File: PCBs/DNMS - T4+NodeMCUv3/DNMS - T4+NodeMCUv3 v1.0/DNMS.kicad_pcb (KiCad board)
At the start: 2 copper layers, 61 x 32.5 mm, 20 parts, among them J1 Conn_02x03_Odd_Even, J2 Conn_01x02, J3 Conn_01x04, J4 Conn_01x05, U2 NodeMCU V3, U3 Teensy4.0

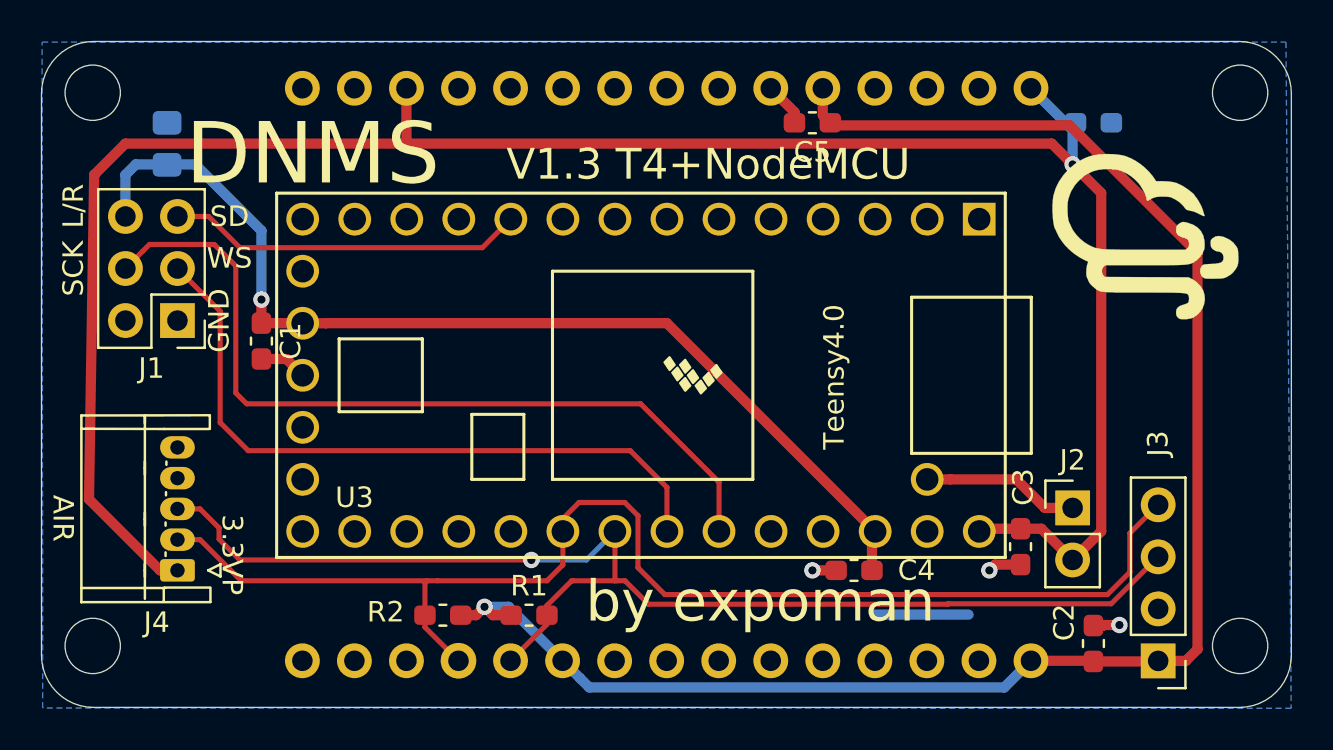
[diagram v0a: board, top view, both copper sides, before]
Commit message: move connectors
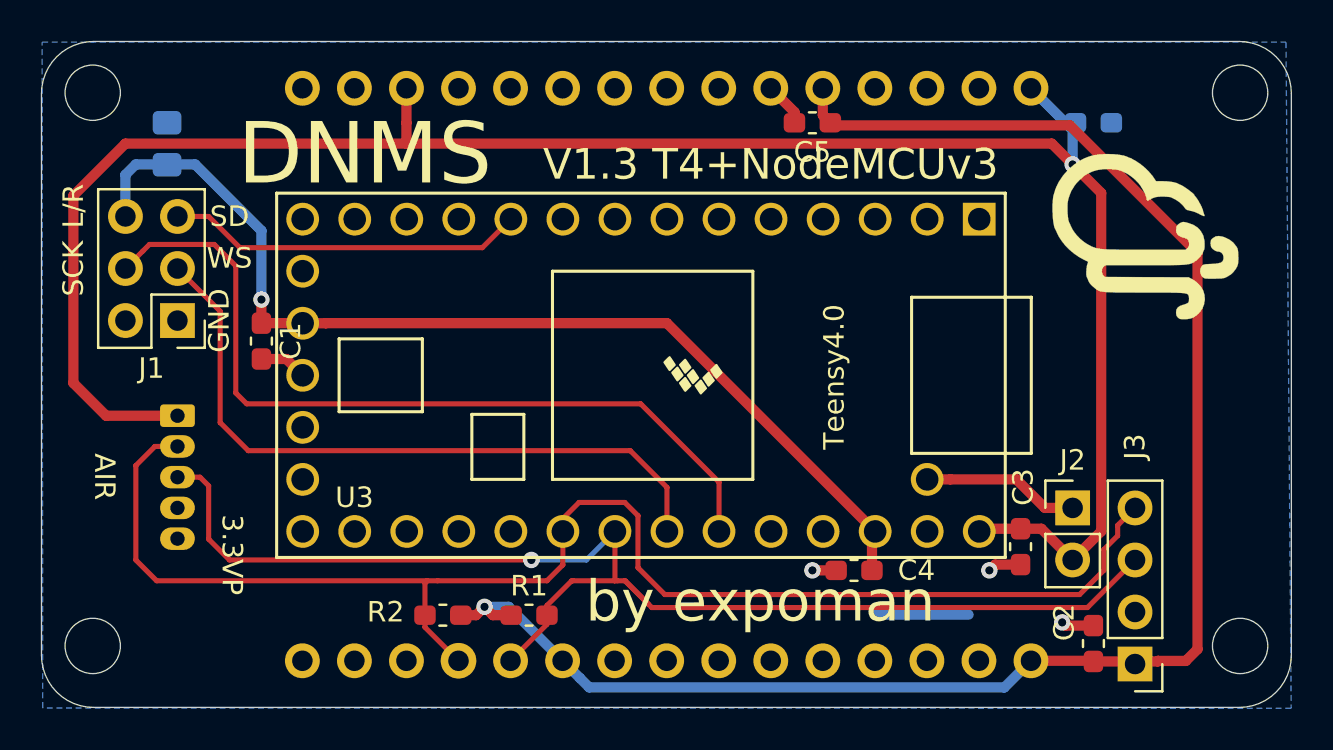
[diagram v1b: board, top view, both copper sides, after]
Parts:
- J4: moved to B.Cu
- moved J4 7.55 mm to (72.1, 75.8), turned to 270 degrees
- moved J3 1.14 mm to (118.9, 87.9)
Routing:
- net SDA: track 62.5 -> 69.7 mm
- net +5V: track 103.8 -> 98.5 mm
- net SCL: track 61.3 -> 63.7 mm
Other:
- board text added: "V1.3 T4+NodeMCUv3"
- board text removed: "V1.3 T4+NodeMCU"

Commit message: change connector to mic to molex pico-ezmate
move other connectors around
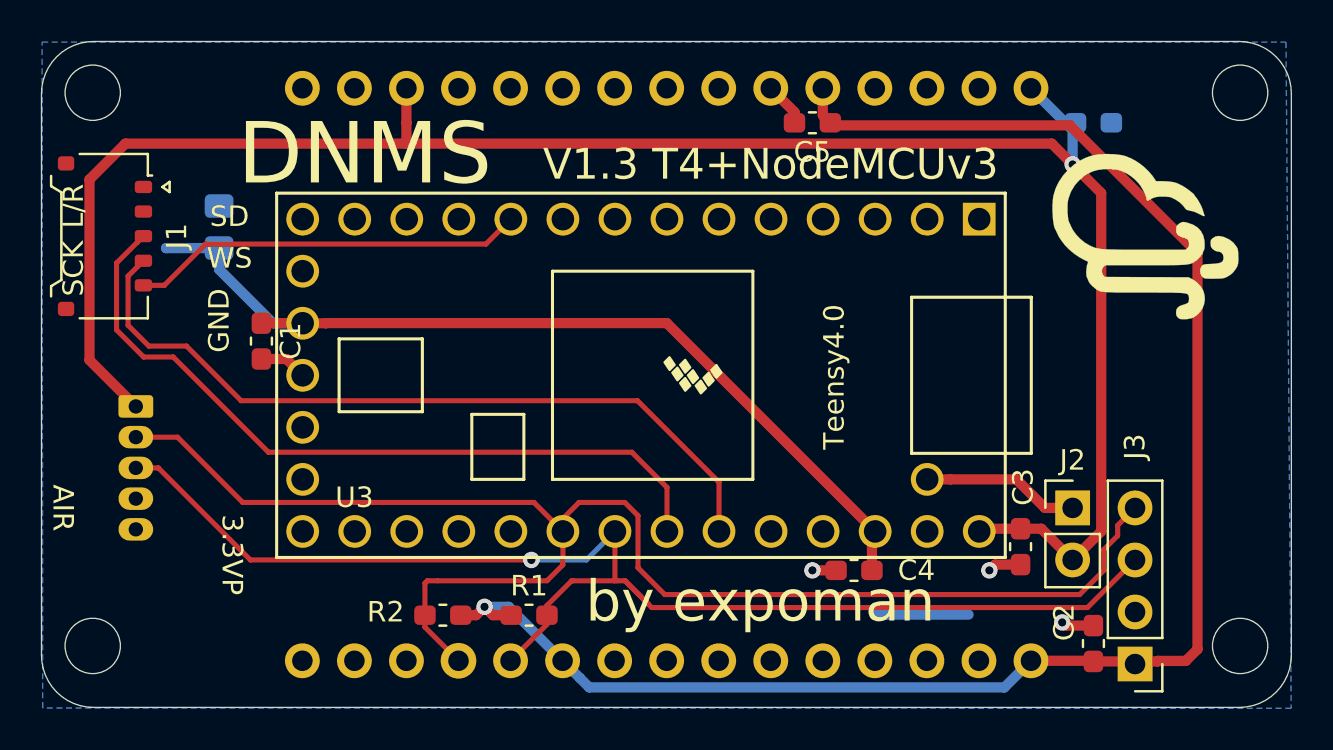
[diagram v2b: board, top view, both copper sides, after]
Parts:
- J1: value Conn_02x03_Odd_Even -> Conn_01x06; footprint Connector_PinHeader_2.54mm:PinHeader_2x03_P2.54mm_Vertical -> Connector_Molex:Molex_Pico-EZmate_78171-0005_1x05-1MP_P1.20mm_Vertical
- moved J1 5.43 mm to (68.6, 67.0), turned to 270 degrees
- moved C6 4.79 mm to (74.2, 66.6)
- moved J4 2.08 mm to (70.1, 75.3)
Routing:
- net +3.3VP: track 50.9 -> 45.0 mm, vias 1 -> 0
- net +5V: track 98.5 -> 94.5 mm
- net WS: track 33.6 -> 37.3 mm
- net SCK: track 40.3 -> 37.9 mm
- net SD: track 17.5 -> 19.3 mm
- net SDA: track 69.7 -> 70.8 mm
- net SCL: track 63.7 -> 64.4 mm

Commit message: add 2.54mm connector headers next to pico ezmate connectors
for backwards compability

moved text around and cleaned design

added additional capcitors
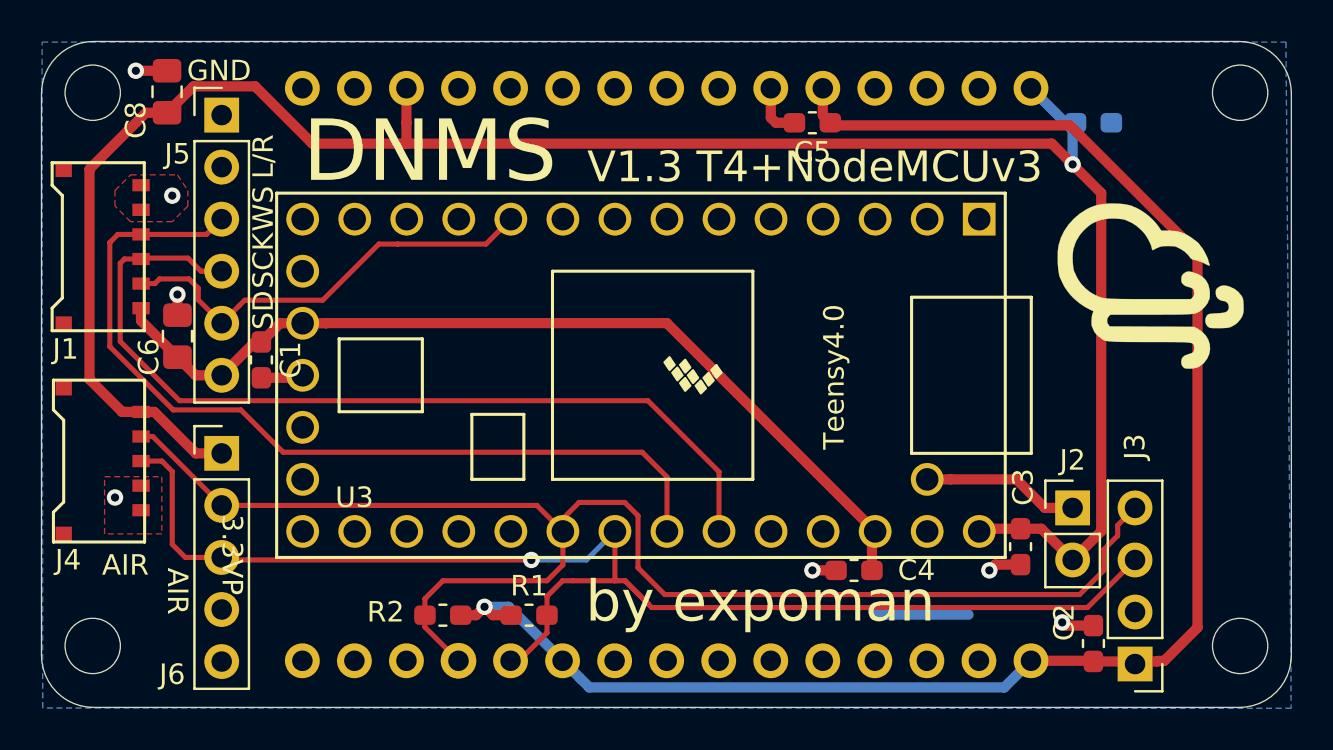
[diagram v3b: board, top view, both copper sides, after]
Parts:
- added C8: 10uF, Capacitor_SMD:C_0805_2012Metric_Pad1.15x1.40mm_HandSolder, F.Cu at (71.6, 60.0)
- added J5: Conn_01x06, Connector_PinHeader_2.54mm:PinHeader_1x06_P2.54mm_Vertical, F.Cu at (74.3, 61.1)
- added J6: Conn_01x05, Connector_PinHeader_2.54mm:PinHeader_1x05_P2.54mm_Vertical, F.Cu at (74.3, 77.6)
- C6: moved to F.Cu
- J1: footprint Connector_Molex:Molex_Pico-EZmate_78171-0005_1x05-1MP_P1.20mm_Vertical -> Connector_Molex:molex_pico-ezmate_781715006_1x06_P1.20mm_Horizontal
- J4: footprint Connector_JST_ZH:JST_ZH_S5B-EH_1x05_P1.50mm_Horizontal -> Connector_Molex:Molex_Pico-EZmate_78171-0005_1x05-1MP_P1.20mm_Horizontal; moved to F.Cu
- moved C6 5.70 mm to (72.1, 71.9)
- moved J4 4.42 mm to (66.6, 78.0)
- moved G*** 2.43 mm to (119.6, 69.5)
- moved J1 2.08 mm to (66.6, 67.5)
- moved C1 0.92 mm to (76.2, 73.0)
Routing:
- net +5V: track 94.5 -> 102.8 mm
- net WS: track 37.3 -> 43.5 mm
- net SCK: track 37.9 -> 43.9 mm
- net GND: track 13.5 -> 16.2 mm, vias 3 -> 7
- net SCL: track 64.4 -> 66.8 mm
- net SD: track 19.3 -> 21.5 mm
- net SDA: track 70.8 -> 70.1 mm
- net +3V3: track 82.0 -> 81.3 mm
- added copper zone on F.Cu, net GND

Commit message: smaller changes to pcb
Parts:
- moved C2 0.51 mm to (116.3, 86.9)
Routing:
- net +3V3: track 81.3 -> 83.6 mm
- net +5V: track 102.8 -> 104.2 mm
- net SCL: track 66.8 -> 66.3 mm

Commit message: smaller pcb changes
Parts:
- C7: moved to F.Cu
- moved C7 2.29 mm to (116.7, 63.8)
- moved G*** 1.65 mm to (119.6, 71.1)
- moved C4 0.53 mm to (105.3, 83.8)
- moved C3 0.25 mm to (113.5, 82.2)
- moved C6 0.25 mm to (71.9, 71.9)
- moved J5 0.13 mm to (74.2, 61.1)
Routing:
- net GND: track 15.9 -> 17.6 mm, vias 7 -> 8
- net +5V: track 104.2 -> 102.6 mm
- net +3V3: track 83.6 -> 84.7 mm
- net SDA: track 69.7 -> 70.7 mm
- net +3.3VP: track 44.8 -> 45.7 mm
